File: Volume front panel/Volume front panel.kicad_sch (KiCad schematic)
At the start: 44 parts, among them IC1 MC7805BD2TR4G, IC2 TLC5947DAPR, IC3 MC7805BD2TR4G, J1 26-60-4023, J2 26-60-4023, J3 4328, U1 PEC11R-4330F-S0012, U2 TSOP39238, U3 ISO1541

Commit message: moving everything onto front panel, switching psu, no iso
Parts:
- removed C10, C16: 10uf, Capacitor_SMD:C_1206_3216Metric, symbol Device:C_Small
- removed C11, C17: 1uf, Capacitor_SMD:C_1206_3216Metric, symbol Device:C_Small
- removed C13, C3: UUD1V101MNL1GS, Samacsys:CAPAE830X1050N, symbol Samacsys_kicad_sym:UUD1V101MNL1GS
- removed C14, C4: .1uf, Capacitor_SMD:C_1206_3216Metric, symbol Device:C_Small
- removed H1, H2: MountingHole, MountingHole:MountingHole_3.2mm_M3_ISO7380, symbol Mechanical:MountingHole
- removed IC1, IC3: MC7805BD2TR4G, Samacsys:TO254P1420X457-4N, symbol Samacsys:MC7805BD2TR4G
- removed J2: 26-60-4023, Samacsys:26604023, symbol Samacsys:26-60-4023
- removed J3: 4328, Snapeda_8:ADAFRUIT_4328, symbol Snapeda_kicad_sym:4328
- removed R10, R5, R6, R9: 1k, Resistor_SMD:R_1206_3216Metric, symbol Device:R_Small
- removed U3: ISO1541, Package_SO:SOIC-8_3.9x4.9mm_P1.27mm, symbol Isolator:ISO1541
- added C12: 0.1uf, Capacitor_SMD:C_1206_3216Metric, symbol Device:C_Small
- added C7, C9: UUD1V101MNL1GS, Samacsys:CAPAE830X1050N, symbol Samacsys_kicad_sym:UUD1V101MNL1GS
- added IC2: TPIC6B595DWR, Samacsys:SOIC127P1030X265-20N, symbol Samacsys_kicad_sym:TPIC6B595DWR
- added J2: 10129381-908001BLF, Samacsys:10129381908001BLF, symbol Samacsys:10129381-908001BLF
- added L1: 150uh, Inductor_SMD:L_Bourns_SRR1260, symbol Device:L
- added PS2: TMPW_5-105, Samacsys:TMPW5112, symbol Samacsys:TMPW_5-105
- added R7: 10k, Resistor_SMD:R_1206_3216Metric, symbol Device:R_Small
- renumbered C12 to C10, C15 to C11, C5 to C3, C6 to C4, C7 to C5, C8 to C6, C9 to C8, H3 to H1, H4 to H2, H5 to H3, H6 to H4, IC2 to IC1, R7 to R5, R8 to R6
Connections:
- net +5V: now also C12.1, C9.1 (+), IC2.2 (VCC), J2.1, J2.2, L1.2, R7.1
- net GNDD: now also C12.2, C7.2 (-), C9.2 (-), IC2.10 (GND_1), IC2.11 (GND_2), IC2.19 (GND_3), PS2.3 (-VOUT); no longer J1.2
- net at J1.1: now also PS2.5 (AC_IN_(N))
- net at C3.2, R1.2: now also A1.5 (D2); no longer A1.6 (D3)
- net at C4.1, U1.2 (NO): now also A1.7 (D4); no longer A1.8 (D5)
- net at C8.1, U2.3 (OUT): now also A1.8 (D5); no longer A1.9 (D6)
- net at C5.1, R4.2: now also A1.6 (D3); no longer A1.7 (D4)
- net unmute: now reaches A1.10 (D7)
- net unmute: now also IC2.9 (~{G})
- net shift_reg_strobe: now reaches A1.11 (D8)
- net shift_reg_strobe: now also IC2.13 (SRCK)
- net shift_reg_clock: now reaches A1.12 (D9)
- net shift_reg_clock: now also IC2.12 (RCK)
- net SCL: no longer names the net of A1.24 (A5)
- net SDA: no longer names the net of A1.23 (A4)
- new net: C7.1 (+), L1.1, PS2.2 (+VOUT)
- new net: IC2.8 (~{SRCLR}), R7.2
- new net: J1.2, PS2.4 (AC_IN_(L))
- new net r0: IC2.4 (DRAIN0), J2.4
- new net r1: IC2.5 (DRAIN1), J2.6
- new net r2: IC2.6 (DRAIN2), J2.8
- new net r3: IC2.7 (DRAIN3), J2.3
- new net r4: IC2.15 (DRAIN5), J2.5
- new net r5: IC2.14 (DRAIN4), J2.7
- new net r_data: A1.9 (D6), IC2.3 (SER_IN)
- no-connect marks 9 -> 11
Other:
- moved on the sheet: J1

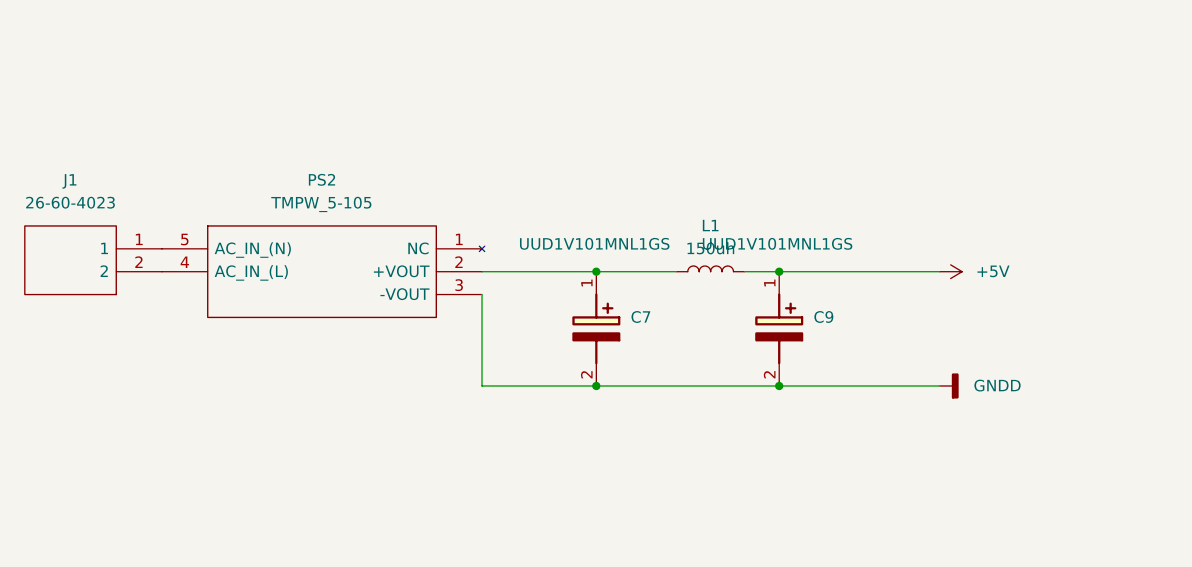
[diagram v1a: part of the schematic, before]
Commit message: seperate psu, traco. All logic and such on front panel
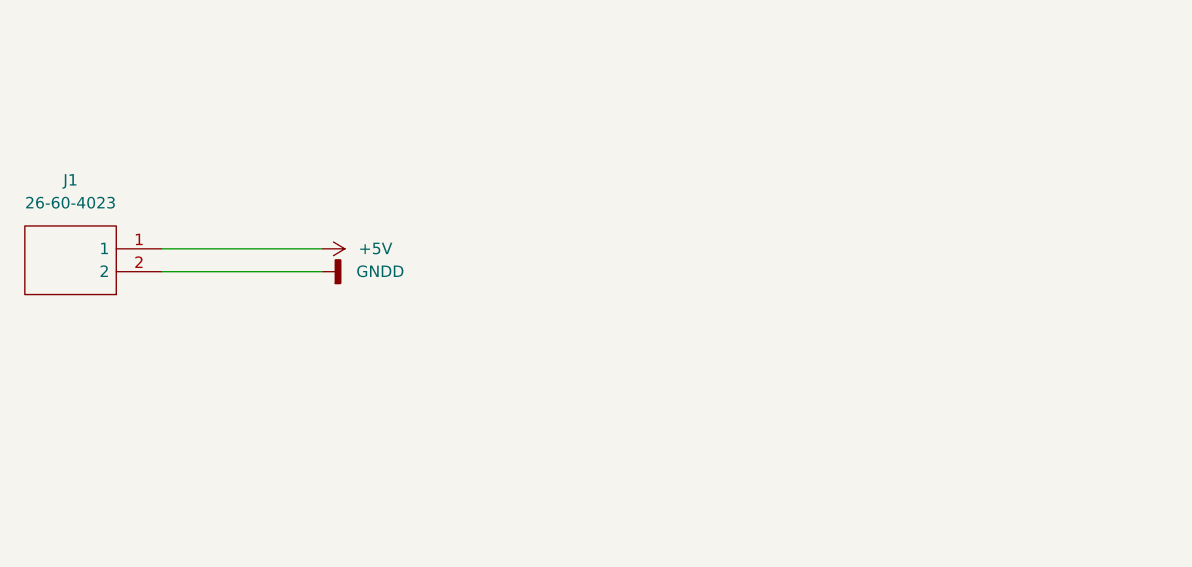
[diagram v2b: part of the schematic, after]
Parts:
- removed C7, C9: UUD1V101MNL1GS, Samacsys:CAPAE830X1050N, symbol Samacsys_kicad_sym:UUD1V101MNL1GS
- removed L1: 150uh, Inductor_SMD:L_Bourns_SRR1260, symbol Device:L
- removed PS2: TMPW_5-105, Samacsys:TMPW5112, symbol Samacsys:TMPW_5-105
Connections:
- net +5V: now also J1.1
- net GNDD: now also J1.2

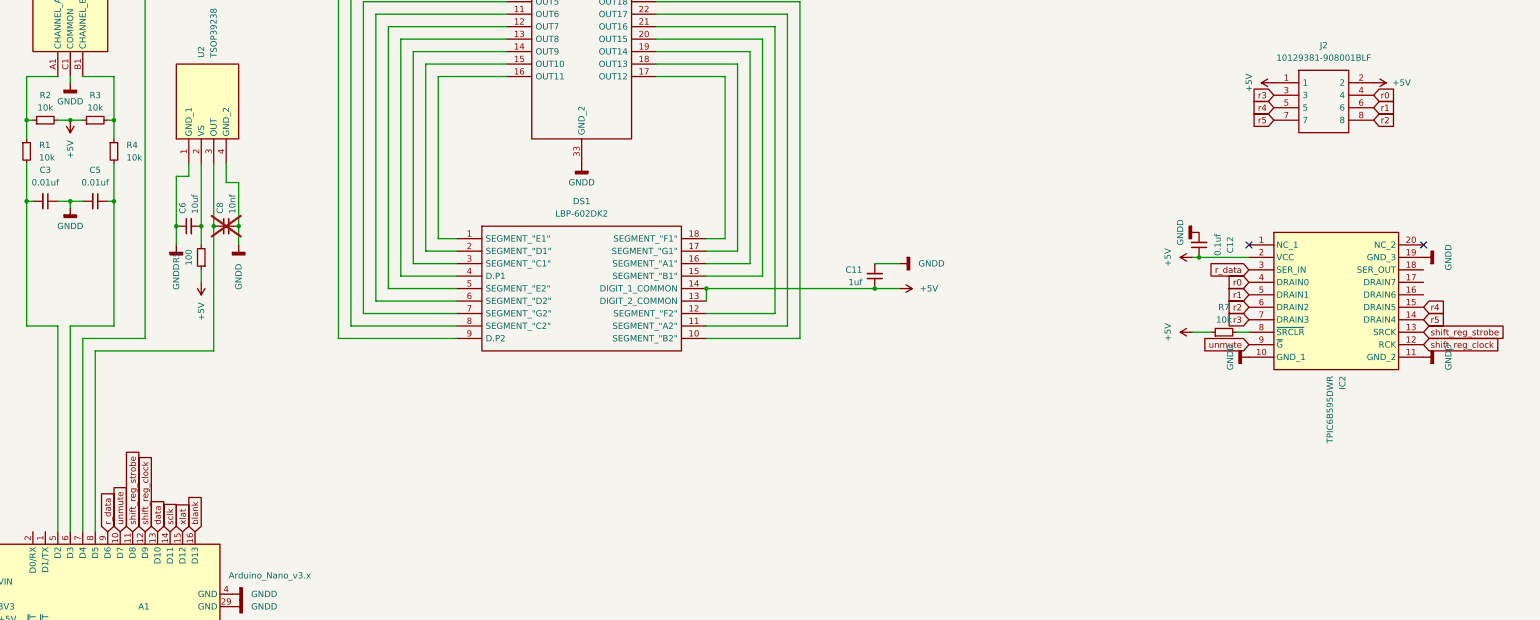
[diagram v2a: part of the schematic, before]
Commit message: audio board, using rlxpassive base
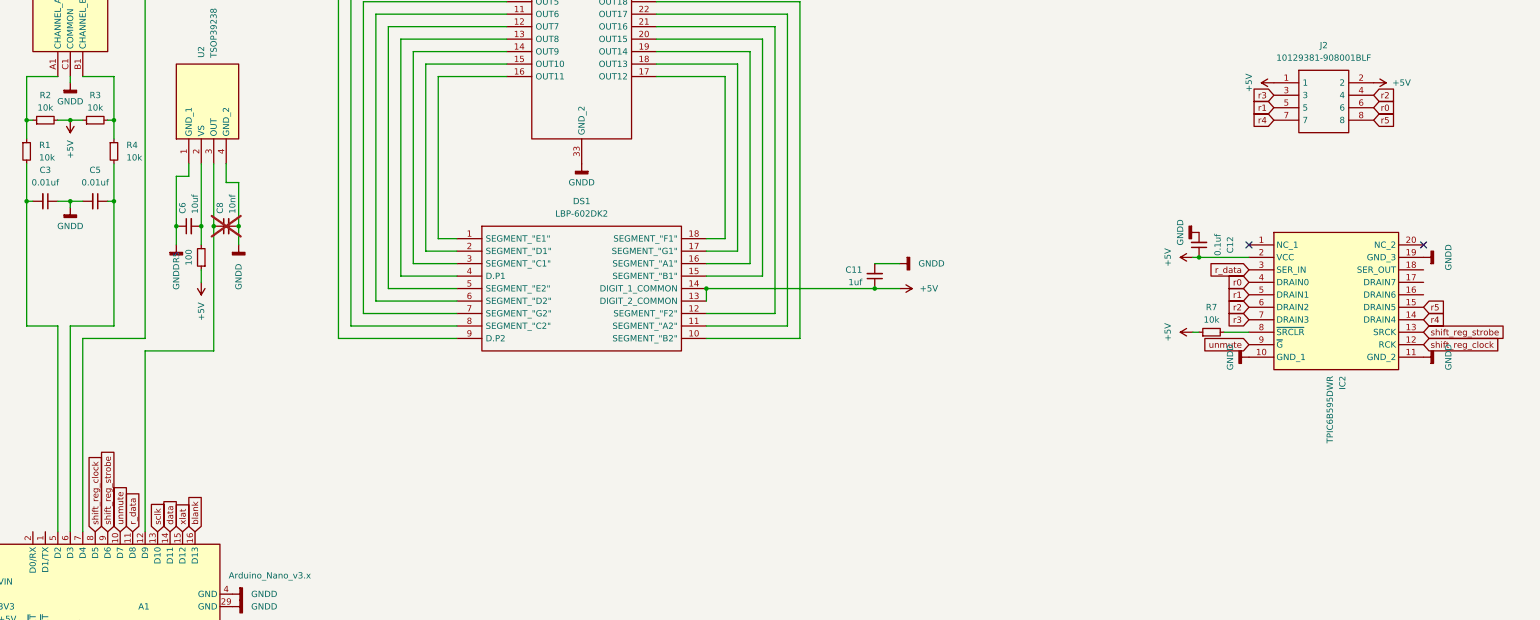
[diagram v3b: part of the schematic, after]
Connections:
- net data: now also A1.14 (D11); no longer A1.13 (D10)
- net r0: now also J2.6; no longer J2.4
- net r1: now also J2.5; no longer J2.6
- net r2: now also J2.4; no longer J2.8
- net r4: now also IC2.14 (DRAIN4), J2.7; no longer IC2.15 (DRAIN5), J2.5
- net r5: now also IC2.15 (DRAIN5), J2.8; no longer IC2.14 (DRAIN4), J2.7
- net r_data: now also A1.11 (D8); no longer A1.9 (D6)
- net sclk: now also A1.13 (D10); no longer A1.14 (D11)
- net shift_reg_clock: now also A1.8 (D5); no longer A1.12 (D9)
- net shift_reg_strobe: now also A1.9 (D6); no longer A1.11 (D8)
- net at C8.1, U2.3 (OUT): now also A1.12 (D9); no longer A1.8 (D5)
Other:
- moved on the sheet: R7

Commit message: likely all done with v1, mainboard obsolete
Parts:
- removed C12: 0.1uf, Capacitor_SMD:C_1206_3216Metric, symbol Device:C_Small
- removed H1, H2, H3, H4: MountingHole, MountingHole:MountingHole_3.2mm_M3_ISO7380, symbol Mechanical:MountingHole
- removed IC2: TPIC6B595DWR, Samacsys:SOIC127P1030X265-20N, symbol Samacsys_kicad_sym:TPIC6B595DWR
- removed J1: 26-60-4023, Samacsys:26604023, symbol Samacsys:26-60-4023
- removed J2: 10129381-908001BLF, Samacsys:10129381908001BLF, symbol Samacsys:10129381-908001BLF
- removed R7: 10k, Resistor_SMD:R_1206_3216Metric, symbol Device:R_Small
- added C2, C3, C5: 0.01uf, Capacitor_SMD:C_1206_3216Metric, symbol Device:C_Small
- added J1, J2: BHR-06-VUA, Samacsys:SHDR6W64P254_2X3_1522X880X920P, symbol Samacsys:BHR-06-VUA
- added R1, R12, R2, R3, R4: 10k, Resistor_SMD:R_1206_3216Metric, symbol Device:R_Small
- added R11, R9: 4.7k, Resistor_SMD:R_1206_3216Metric, symbol Device:R_Small
- added U1: PEC11R-4330F-S0012, Samacsys:PEC11R4330FS0012, symbol Samacsys_kicad_sym:PEC11R-4330F-S0012
- renumbered C8 to C10, C10 to C11, C11 to C12, C2 to C4, C3 to C6, C4 to C7, C5 to C8, C6 to C9, R5 to R10, R6 to R13, R1 to R5, R2 to R6, R3 to R7, R4 to R8, U1 to U2, U2 to U3
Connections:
- net r_data is gone; now on net IR: A1.11 (D8)
- net shift_reg_clock is gone; now on an unnamed net: A1.8 (D5)
- net unmute is gone; now on an unnamed net: A1.10 (D7)
- net +5V: now also J1.1, J1.3, J1.5, J2.1, J2.2, R11.2, R2.2, R3.1, R9.2
- net GNDD: now also C2.1, C3.2, C5.2, J1.2, J1.4, J1.6, J2.3, J2.4, R12.1, U1.1 (COM), U1.C1 (COMMON)
- net blank: now also A1.21 (A2), R12.2; no longer A1.16 (D13)
- net data: now also A1.19 (A0); no longer A1.14 (D11)
- net sclk: now also A1.20 (A1); no longer A1.13 (D10)
- net xlat: now also A1.22 (A3); no longer A1.15 (D12)
- net at C7.1, U2.2 (NO): no longer A1.7 (D4)
- net IR: now reaches C10.1, U3.3 (OUT)
- net IR: no longer A1.12 (D9)
- net at C8.1, R8.2: no longer A1.6 (D3)
- net SDA: now reaches A1.23 (A4)
- net SDA: now also J2.6, R9.1
- net SCL: now reaches A1.24 (A5)
- net SCL: now also J2.5, R11.1
- net shift_reg_strobe: no longer names the net of A1.9 (D6)
- net shift_reg_strobe: now also C3.1, U1.2 (NO)
- new net: A1.6 (D3), C2.2, R1.2
- new net: R3.2, R4.1, U1.B1 (CHANNEL_B)
- new net: R1.1, R2.1, U1.A1 (CHANNEL_A)
- new net: A1.7 (D4), C5.1, R4.2

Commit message: almost made 2040 raw
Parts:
- removed A1: Arduino_Nano_v3.x, Module:Arduino_Nano, symbol MCU_Module:Arduino_Nano_v3.x
- removed C1: UUD1V101MNL1GS, Samacsys:CAPAE830X1050N, symbol Samacsys_kicad_sym:UUD1V101MNL1GS
- removed C4: .1uf, Capacitor_SMD:C_1206_3216Metric, symbol Device:C_Small
- removed J1, J2: BHR-06-VUA, Samacsys:SHDR6W64P254_2X3_1522X880X920P, symbol Samacsys:BHR-06-VUA
- removed R9: 4.7k, Resistor_SMD:R_1206_3216Metric, symbol Device:R_Small
- added C2, C8: 15p, Capacitor_SMD:C_1206_3216Metric, symbol Device:C_Small
- added C5: 10uf, Capacitor_SMD:C_1206_3216Metric, symbol Device:C_Small
- added IC1: W25Q16JVUXIQ_TR, Samacsys:SON50P300X200X60-9N, symbol Samacsys:W25Q16JVUXIQ_TR
- added IC2: TS02-66-80-BK-160-LCR-D, Samacsys:TS026680BK160LCRD, symbol Samacsys:TS02-66-80-BK-160-LCR-D
- added J1: 10159872-00011LF, Samacsys:1015987200011LF, symbol Samacsys:10159872-00011LF
- added R1, R2: 5.1k, Resistor_SMD:R_1206_3216Metric, symbol Device:R_Small
- added R15, R16: 27.4, Resistor_SMD:R_1206_3216Metric, symbol Device:R_Small
- added R3: 1k, Resistor_SMD:R_1206_3216Metric, symbol Device:R_Small
- added R4: 10k, Resistor_SMD:R_1206_3216Metric, symbol Device:R_Small
- added U4: MIC5205-3.3YM5, Package_TO_SOT_SMD:SOT-23-5, symbol Regulator_Linear:MIC5205-3.3YM5
- added U5: RP2040, Package_DFN_QFN:QFN-56-1EP_7x7mm_P0.4mm_EP3.2x3.2mm, symbol MCU_RaspberryPi:RP2040
- added Y1: ABM8-12.000MHZ-B2-T, Samacsys:ABM810000MHZ12D2W, symbol Samacsys:ABM8-12.000MHZ-B2-T
- R11: value 4.7k -> 1k
- renumbered C2 to C1, C9 to C10, C10 to C11, C11 to C12, C12 to C13, C5 to C4, C8 to C9, IC1 to IC3, R6 to R10, R7 to R12, R8 to R13, R10 to R14, R12 to R17, R13 to R18, R1 to R5, R2 to R6, R3 to R7, R4 to R8, R5 to R9
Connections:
- net +5V: now also U4.1 (IN), U4.3 (EN); no longer R10.2, R11.2, R12.1, R14.1, R6.2, R7.1
- net GNDD: now also C2.1, C5.2, C8.1, IC1.4 (GND), IC1.9 (EP), IC2.2 (NO_2), J1.A1 (GND_1), J1.A12 (GND_2), J1.B1 (GND_3), J1.B12 (GND_4), R1.1, R2.1, U4.2 (GND), U4.4 (BP), U5.19 (TESTEN), U5.57 (GND), Y1.2 (GND_1), Y1.4 (GND_2)
- net IR: now also U5.34 (GPIO22)
- net blank: now also U5.14 (GPIO11)
- net data: now also U5.11 (GPIO8)
- net sclk: now also U5.12 (GPIO9)
- net xlat: now also U5.13 (GPIO10)
- net enc1a: now reaches C1.2, R5.2
- net enc1a: now also U5.27 (GPIO16)
- net enc1press: now reaches C3.1, U1.2 (NO)
- net enc1press: now also U5.31 (GPIO20)
- net enc1b: now reaches C4.1, R8.2
- net enc1b: now also U5.28 (GPIO17)
- net enc2a: now reaches C6.2, R9.2
- net enc2a: now also U5.29 (GPIO18)
- net enc2press: now reaches C7.1, U2.2 (NO)
- net enc2press: now also U5.32 (GPIO21)
- net enc2b: now reaches C9.1, R13.2
- net enc2b: now also U5.30 (GPIO19)
- net SCL: no longer names the net of R11.1
- net SCL: now also C8.2, Y1.3 (X2)
- new net: IC1.1 (~{CS}), R3.2, R4.1
- new net: J1.A5 (CC1), R1.2
- new net: J1.B5 (CC2), R2.2
- new net: U5.23 (DVDD), U5.45 (VREG_VOUT), U5.50 (DVDD)
- new net: R16.1, U5.46 (USB_DM)
- new net: R15.1, U5.47 (USB_DP)
- new net +3.3V: C5.1, IC1.8 (VCC), R10.2, R12.1, R14.1, R4.2, R6.2, R7.1, U4.5 (OUT), U5.1 (IOVDD), U5.10 (IOVDD), U5.22 (IOVDD), U5.33 (IOVDD), U5.42 (IOVDD), U5.43 (ADC_AVDD), U5.44 (VREG_IN), U5.48 (USB_VDD), U5.49 (IOVDD)
- new net CLR1: U5.18 (GPIO15)
- new net QSPI_SCLK: IC1.6 (CLK), U5.52 (QSPI_SCLK)
- new net QSPI_SD0: IC1.2 (DO(IO1)), U5.53 (QSPI_SD0)
- new net QSPI_SD1: IC1.5 (DI(IO0)), U5.55 (QSPI_SD1)
- new net QSPI_SD2: IC1.3 (IO2), U5.54 (QSPI_SD2)
- new net QSPI_SD3: IC1.7 (IO3), U5.51 (QSPI_SD3)
- new net QSPI_SS: IC2.4 (COM_2), R3.1, U5.26 (RUN), U5.56 (QSPI_SS)
- new net RCLK1: U5.17 (GPIO14)
- new net SER1: U5.15 (GPIO12)
- new net SRCLK1: U5.16 (GPIO13)
- new net XIN: C2.2, R11.2, U5.20 (XIN), U5.21 (XOUT), Y1.1 (X1)
- new net dm: J1.A7 (DN1), J1.B7 (DN2), R16.2
- new net dp: J1.A6 (DP1), J1.B6 (DP2), R15.2
- no-connect marks 11 -> 33
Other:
- moved on the sheet: C1, C10, C11, C12, C13, C3, C4, C6, C7, C9, DS1, IC3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

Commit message: pico front panel so easy
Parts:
- removed C2, C8: 15p, Capacitor_SMD:C_1206_3216Metric, symbol Device:C_Small
- removed C5: 10uf, Capacitor_SMD:C_1206_3216Metric, symbol Device:C_Small
- removed IC1: W25Q16JVUXIQ_TR, Samacsys:SON50P300X200X60-9N, symbol Samacsys:W25Q16JVUXIQ_TR
- removed IC2: TS02-66-80-BK-160-LCR-D, Samacsys:TS026680BK160LCRD, symbol Samacsys:TS02-66-80-BK-160-LCR-D
- removed J1: 10159872-00011LF, Samacsys:1015987200011LF, symbol Samacsys:10159872-00011LF
- removed R1, R2: 5.1k, Resistor_SMD:R_1206_3216Metric, symbol Device:R_Small
- removed R11, R3: 1k, Resistor_SMD:R_1206_3216Metric, symbol Device:R_Small
- removed R15, R16: 27.4, Resistor_SMD:R_1206_3216Metric, symbol Device:R_Small
- removed R4: 10k, Resistor_SMD:R_1206_3216Metric, symbol Device:R_Small
- removed U4: MIC5205-3.3YM5, Package_TO_SOT_SMD:SOT-23-5, symbol Regulator_Linear:MIC5205-3.3YM5
- removed U5: RP2040, Package_DFN_QFN:QFN-56-1EP_7x7mm_P0.4mm_EP3.2x3.2mm, symbol MCU_RaspberryPi:RP2040
- removed Y1: ABM8-12.000MHZ-B2-T, Samacsys:ABM810000MHZ12D2W, symbol Samacsys:ABM8-12.000MHZ-B2-T
- added J1: TFM-105-01-F-D, Samacsys:TFM-105-XX-YYY-D, symbol Samacsys:TFM-105-01-F-D
- added J2: 26-60-4023, Samacsys:26604023, symbol Samacsys:26-60-4023
- added PS1: TMPW_5-105, Samacsys:TMPW5112, symbol Samacsys_kicad_sym:TMPW_5-105
- added U4: Pico, MCU_RaspberryPi_and_Boards:RPi_Pico_SMD_TH, symbol MCU_RaspberryPi_and_Boards:Pico
- renumbered C13 to C10, C3 to C2, C4 to C3, C6 to C4, C7 to C5, C9 to C6, C10 to C7, C11 to C8, C12 to C9, IC3 to IC1, R5 to R1, R17 to R10, R18 to R11, R6 to R2, R7 to R3, R8 to R4, R9 to R5, R10 to R6, R12 to R7, R13 to R8, R14 to R9
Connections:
- net +3.3V: now also J1.8, U4.36 (3V3)
- net +5V: now also J1.1, J1.2, J1.4, PS1.2 (+VOUT), U4.39 (VSYS)
- net GNDD: now also J1.3, J1.5, J1.6, PS1.3 (-VOUT), U4.13 (GND), U4.18 (GND), U4.23 (GND), U4.28 (GND), U4.3 (GND), U4.33 (AGND), U4.38 (GND), U4.42 (GND), U4.8 (GND)
- net IR: now also U4.20 (GPIO15)
- net RCLK1: now also J1.7, U4.7 (GPIO5)
- net SER1: now also J1.10, U4.10 (GPIO7)
- net SRCLK1: now also J1.9, U4.9 (GPIO6)
- net blank: now also U4.12 (GPIO9)
- net data: now also U4.14 (GPIO10)
- net enc1a: now also U4.1 (GPIO0)
- net enc1b: now also U4.2 (GPIO1)
- net enc1press: now also U4.4 (GPIO2)
- net enc2a: now also U4.17 (GPIO13)
- net enc2b: now also U4.19 (GPIO14)
- net enc2press: now also U4.16 (GPIO12)
- net sclk: now also U4.15 (GPIO11)
- net xlat: now also U4.11 (GPIO8)
- new net: J2.2, PS1.4 (AC_IN_(L))
- new net: J2.1, PS1.5 (AC_IN_(N))
- no-connect marks 33 -> 15

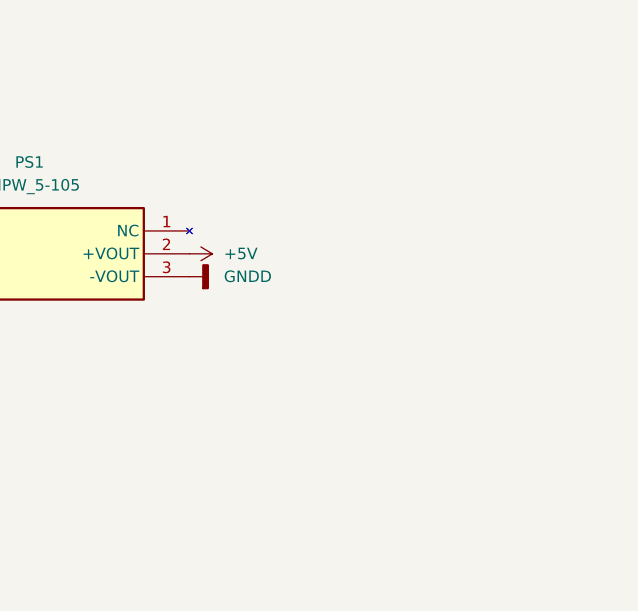
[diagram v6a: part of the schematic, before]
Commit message: moved control to side, added electrolytic caps
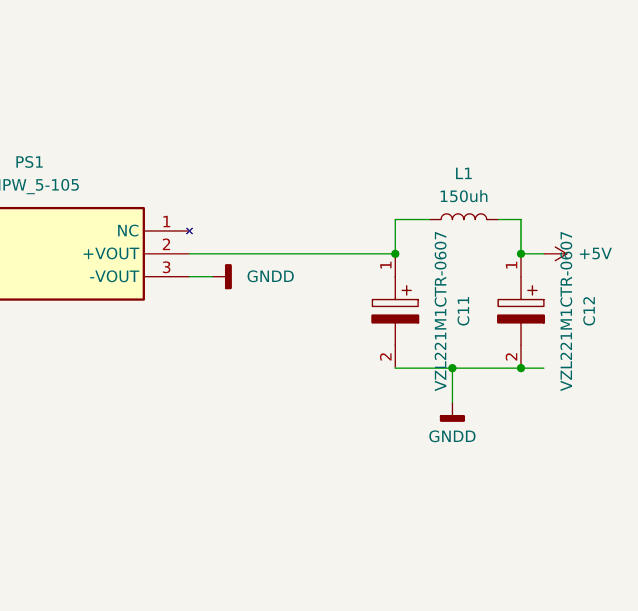
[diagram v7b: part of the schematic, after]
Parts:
- added C11, C12: VZL221M1CTR-0607, Samacsys:CAPAE660X800N, symbol Samacsys:VZL221M1CTR-0607
- added L1: 150uh, Inductor_SMD:L_Coilcraft_XAL6060-XXX, symbol Device:L
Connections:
- net +5V: now also C12.1, L1.2; no longer PS1.2 (+VOUT)
- net GNDD: now also C11.2, C12.2
- new net: C11.1, L1.1, PS1.2 (+VOUT)
